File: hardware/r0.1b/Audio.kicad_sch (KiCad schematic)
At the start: 73 parts, among them IC1 LM4861MX, J1 Kenwood-2.5, J4 CAT_TX, J5 Kenwood-3.5, J6 CAT_RX, J7 Radio, Q1 IRLML2060, U1 MAX9814, U5 MAX3232, U6 MCP602, U7 MCP602, U8 MCP4551-103, U9 MCP4551-104

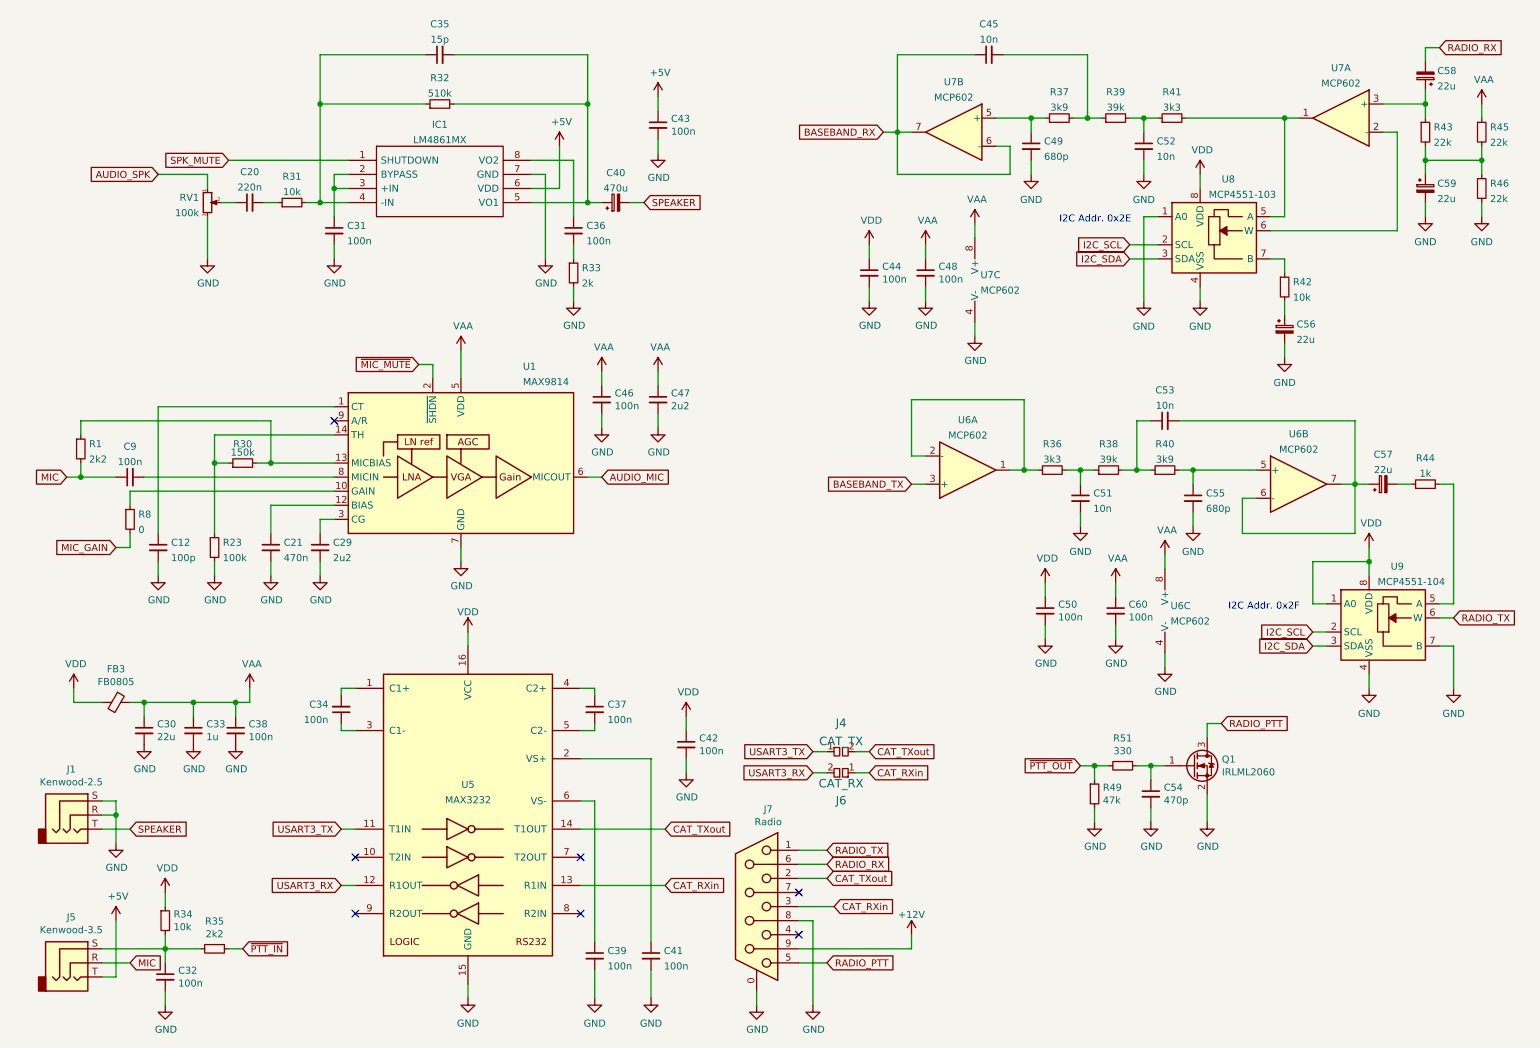
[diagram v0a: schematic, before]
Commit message: Added RTC and Test Points to r0.1b
This marks production for revision 0.1b
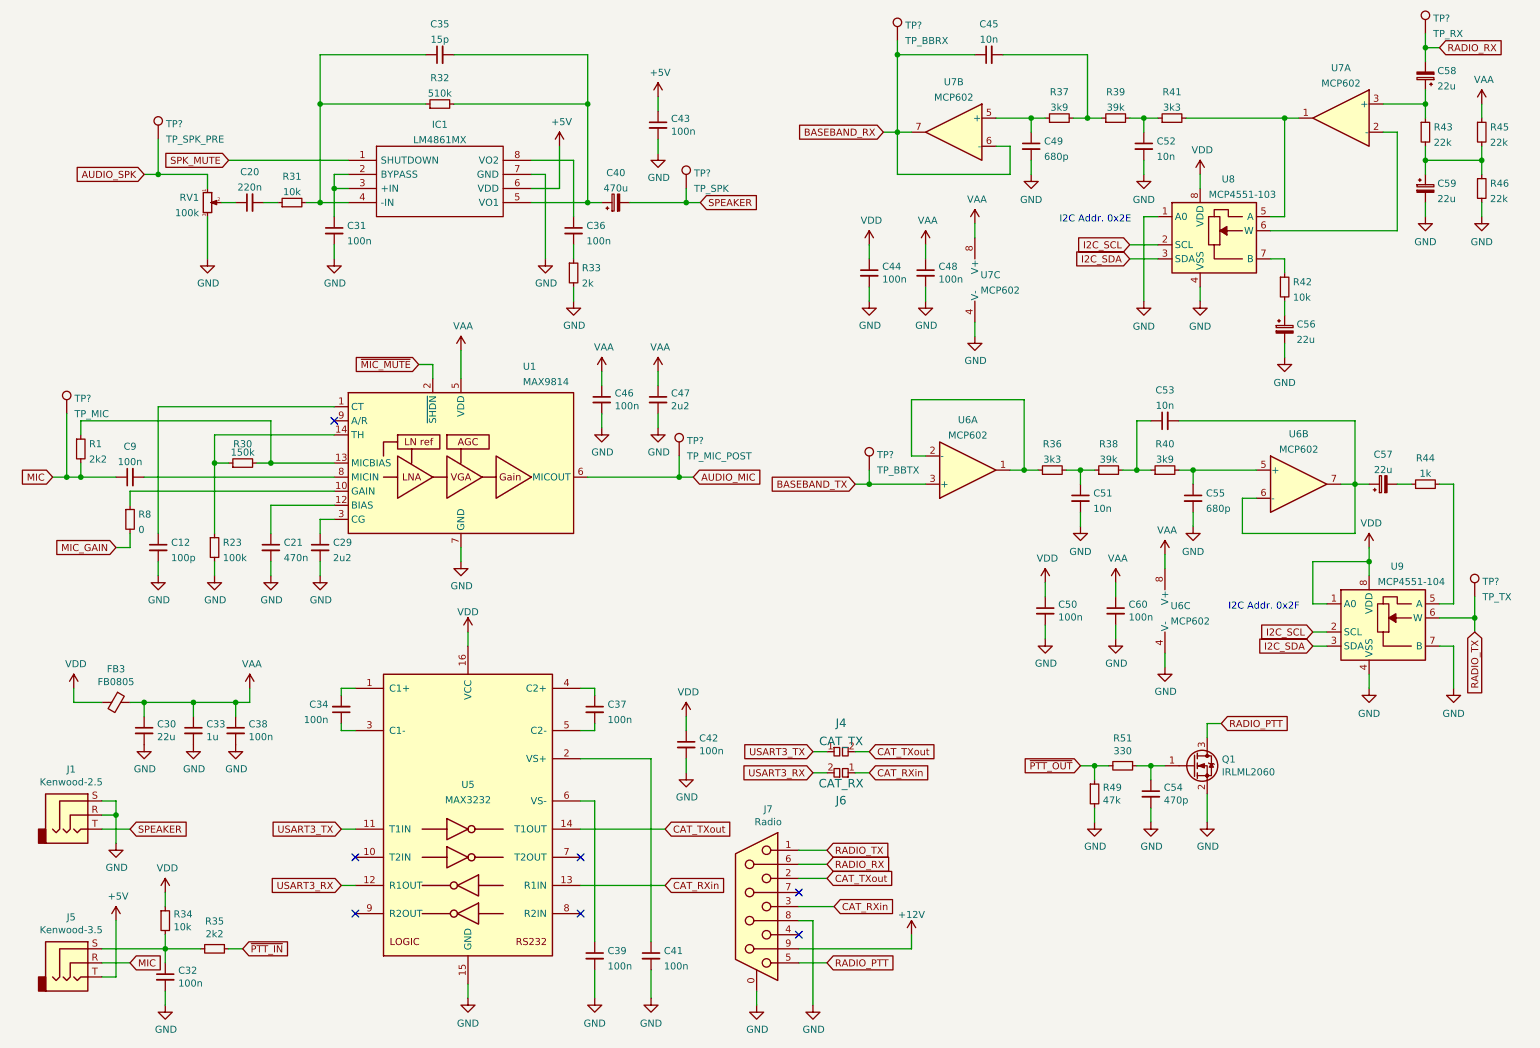
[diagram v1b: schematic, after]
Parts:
- added TP?: TP_MIC, TestPoint:TestPoint_Pad_D1.0mm, symbol Connector:TestPoint
- added TP?: TP_SPK_PRE, TestPoint:TestPoint_Pad_D1.0mm, symbol Connector:TestPoint
- added TP?: TP_BBTX, TestPoint:TestPoint_Pad_D1.0mm, symbol Connector:TestPoint
- added TP?: TP_MIC_POST, TestPoint:TestPoint_Pad_D1.0mm, symbol Connector:TestPoint
- added TP?: TP_BBRX, TestPoint:TestPoint_Pad_D1.0mm, symbol Connector:TestPoint
- added TP?: TP_TX, TestPoint:TestPoint_Pad_D1.0mm, symbol Connector:TestPoint
- added TP?: TP_RX, TestPoint:TestPoint_Pad_D1.0mm, symbol Connector:TestPoint
- added TP?: TP_SPK, TestPoint:TestPoint_Pad_D1.0mm, symbol Connector:TestPoint
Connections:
- net AUDIO_MIC: now also TP?.1
- net AUDIO_SPK: now also TP?.1
- net BASEBAND_RX: now also TP?.1
- net BASEBAND_TX: now also TP?.1
- net MIC: now also TP?.1
- net RADIO_RX: now also TP?.1
- net RADIO_TX: now also TP?.1
- net SPEAKER: now also TP?.1
